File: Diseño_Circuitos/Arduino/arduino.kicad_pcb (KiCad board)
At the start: 2 copper layers, 53.1 x 68.1 mm, 97 parts, among them IC1 FT232RL, J1 Conn_01x10, J10 Conn_01x02, J2 Conn_01x08, J3 Conn_01x06, J4 Conn_01x08, J5 Conn_02x03_Counter_Clockwise, J6 Conn_02x03_Counter_Clockwise, J7 USB_OTG, J8 Conn_01x02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

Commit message: power supply rutted
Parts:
- C12, C17, C18: moved to B.Cu
- moved R24 21.2 mm to (41.7, 79.6), turned to 90 degrees
- moved R11 21.0 mm to (62.1, 105.0), turned to 270 degrees
- moved SW6 20.2 mm to (41.8, 76.5), turned to 90 degrees
- moved R12 16.6 mm to (65.5, 105.1), turned to 90 degrees
- moved C10 14.8 mm to (62.2, 85.8), turned to 180 degrees
- moved R17 14.4 mm to (62.2, 82.5), turned to 180 degrees
- moved C12 10.4 mm to (62.2, 79.2), turned to 180 degrees
- moved R21 10.1 mm to (69.4, 76.5), turned to 90 degrees
- moved R8 8.43 mm to (58.8, 104.9), turned to 270 degrees
- moved C3 8.25 mm to (58.2, 115.2), turned to 90 degrees
- moved R15 8.19 mm to (40.0, 87.8), turned to 180 degrees
- moved C4 7.85 mm to (62.0, 111.6), turned to 0 degrees
- moved D6 7.82 mm to (40.1, 87.6), turned to 180 degrees
- moved C13 6.28 mm to (72.9, 76.4), turned to 270 degrees
- moved J5 6.03 mm to (58.2, 130.6), turned to 0 degrees
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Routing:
- net GND: track 27.3 -> 94.9 mm, vias 15 -> 7
- net +3V3: track 0.00 -> 57.2 mm, vias 0 -> 4
- net BT_TX: track 0.00 -> 49.4 mm, vias 0 -> 2
- net +5V: track 0.00 -> 48.0 mm, vias 0 -> 2
- net BT_RX: track 0.00 -> 47.2 mm
- net +3.3VP: track 0.00 -> 33.9 mm, vias 0 -> 2
- net /RXD: track 0.00 -> 28.0 mm, vias 0 -> 1
- net /TXD: track 0.00 -> 23.7 mm, vias 0 -> 1
- net D-: track 0.00 -> 22.8 mm, vias 0 -> 1
- net D+: track 0.00 -> 21.8 mm, vias 0 -> 1
- net /TXLED: track 0.00 -> 17.9 mm, vias 0 -> 3
- net /RXLED: track 0.00 -> 17.2 mm, vias 0 -> 3
- net +12V: track 0.00 -> 13.6 mm
- net Net-(IC1-Pad17): track 0.00 -> 9.68 mm, vias 0 -> 2
- net Net-(R19-Pad2): track 0.00 -> 8.38 mm
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
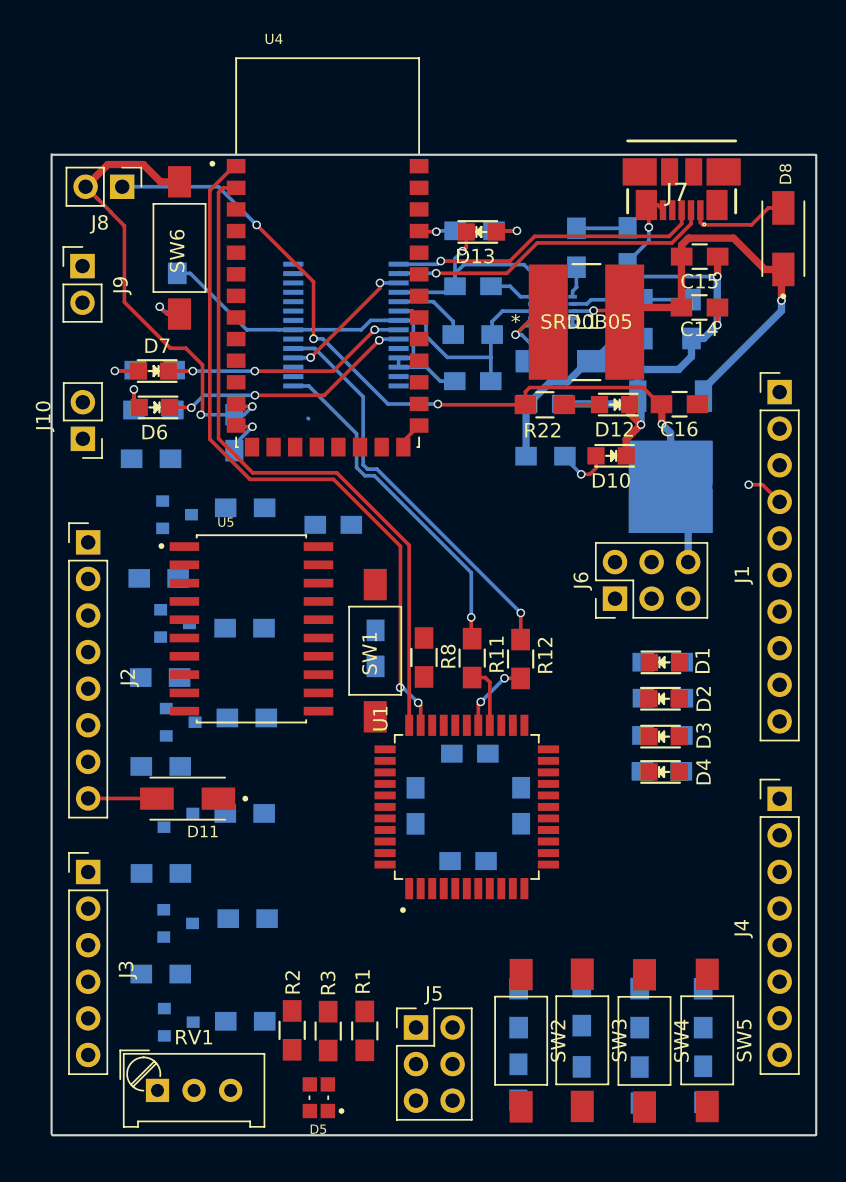
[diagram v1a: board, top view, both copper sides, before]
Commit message: pcb buttons and outputs traced
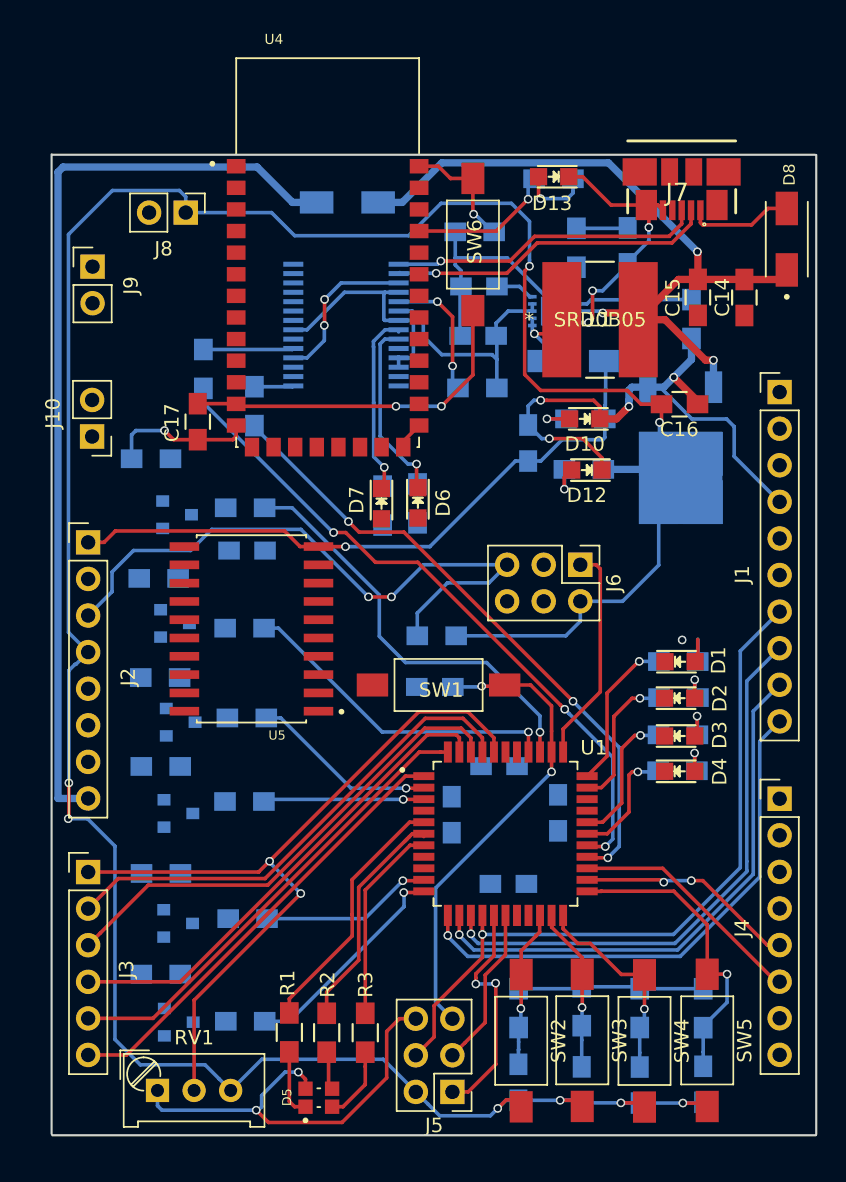
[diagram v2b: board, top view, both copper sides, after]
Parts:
- C17: moved to F.Cu
- D11, R11, R12, R22, R8: moved to B.Cu
- moved D11 42.9 mm to (53.5, 73.4)
- moved R12 29.8 mm to (43.5, 84.9)
- moved R11 23.1 mm to (47.0, 87.5)
- moved R24 21.1 mm to (62.3, 75.4), turned to 180 degrees
- moved SW6 20.4 mm to (62.2, 76.3), turned to 270 degrees
- moved D6 19.5 mm to (58.4, 94.2), turned to 270 degrees
- moved R15 19.5 mm to (58.3, 94.2), turned to 270 degrees
- moved R16 18.4 mm to (55.9, 94.4), turned to 270 degrees
- moved D7 18.3 mm to (55.8, 94.3), turned to 270 degrees
- moved C4 7.37 mm to (68.1, 115.7), turned to 270 degrees
- moved R23 6.57 mm to (67.8, 71.7)
- moved C3 6.42 mm to (64.0, 112.5), turned to 0 degrees
- moved D13 6.31 mm to (67.8, 71.6), turned to 180 degrees
- moved C18 6.25 mm to (46.5, 97.5), turned to 180 degrees
- moved C2 5.50 mm to (64.6, 120.7), turned to 0 degrees
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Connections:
- J5 pad 2: /SCK -> +3V3
- J5 pad 3: /RESET -> /SCK
- J5 pad 4: GND -> /MOSI
- J5 pad 5: /MOSI -> /RESET
- J5 pad 6: +3V3 -> GND
- J6 pad 2: Net-(J6-Pad2) -> +3V3
- J6 pad 3: /RESET -> Net-(J6-Pad3)
- J6 pad 4: GND -> Net-(J6-Pad4)
- J6 pad 5: Net-(J6-Pad5) -> /RESET
- J6 pad 6: +3V3 -> GND
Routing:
- net +3V3: track 57.2 -> 206.7 mm, vias 4 -> 8
- net /RESET: track 0.00 -> 77.5 mm, vias 0 -> 4
- net VIN: track 4.78 -> 64.7 mm
- net GND: track 94.9 -> 150.2 mm, vias 7 -> 10
- net /A0: track 0.00 -> 54.4 mm, vias 0 -> 2
- net /MOSI: track 0.00 -> 50.4 mm, vias 0 -> 1
- net /TXD1: track 5.15 -> 47.3 mm, vias 2 -> 3
- net /RXD1: track 4.35 -> 44.1 mm, vias 0 -> 3
- net /PWM/CS: track 0.00 -> 39.3 mm, vias 0 -> 1
- net BT_TX: track 49.4 -> 10.2 mm, vias 2 -> 1
- net /PWM: track 0.00 -> 38.3 mm, vias 0 -> 1
- net BT_STATE: track 0.00 -> 37.4 mm, vias 0 -> 1
- net BT_RX: track 47.2 -> 10.9 mm, vias 0 -> 1
- net +12V: track 13.6 -> 48.6 mm, vias 0 -> 1
- net /A1: track 0.00 -> 34.4 mm
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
